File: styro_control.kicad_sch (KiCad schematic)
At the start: 89 parts, among them J3 INPUT_PEDAL, Q1 IRF7324, SW1 SW_RESET, SW2 switch_6_pin, SW3 SW_1, SW4 SW_2, SW5 SW_3, U1 STUSB4500QTR, U2 PAC1932-4, U3 ATSAMD21E18A-M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

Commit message: updated schematic
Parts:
- added D? (x3): LED, symbol Device:LED
- added D?: (no value), symbol Device:LED
- added RN?: R_Pack04, Resistor_SMD:R_Array_Convex_4x0603, symbol Device:R_Pack04
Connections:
- net GND: now also D?.1 (K), D?.1 (K), D?.1 (K), D?.1 (K)
- net TX_A6: now also RN?.4 (R4.1)
- net VBUS: now also RN?.1 (R1.1)
- net VSNK: now also RN?.2 (R2.1)
- new net: D?.2 (A), RN?.8 (R1.2)
- new net: D?.2 (A), RN?.7 (R2.2)
- new net: D?.2 (A), RN?.6 (R3.2)
- new net: D?.2 (A), RN?.5 (R4.2)
- new net +3.3V: RN?.3 (R3.1)
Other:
- moved on the sheet: C10, C11, C8, C9, R11, R12, R13, R14, R15, R16, R17, R18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

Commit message: added footprints
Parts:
- D11, D8, D9: renamed from D?; value LED -> (none)
- gave numbers to parts that had none: 3

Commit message: added footprints
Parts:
- added R7, R8: (no value), Resistor_SMD:R_0603_1608Metric, symbol Device:R
- R11, R12, R13, R14, R15, R16, R17, R18, R43, R44, R45, R46: footprint Resistor_SMD:R_0805_2012Metric_Pad1.15x1.40mm_HandSolder -> (none)
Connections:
- net GND: now also R7.1, R8.1; no longer D3.1 (RK), D3.3 (BK)
- new net: D3.1 (RK), R8.2
- new net: D3.3 (BK), R7.2
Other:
- note added: "x footprint von PAC1934 ändern >> größeres qfn!! x I2c Display pin reihenfolge ändern > VDD GND SCK SDA"
- note removed: "x footprint von PAC1934 ändern >> größeres qfn!! I2c Display pin reihenfolge ändern > VDD GND SCK SDA"
- moved on the sheet: D3

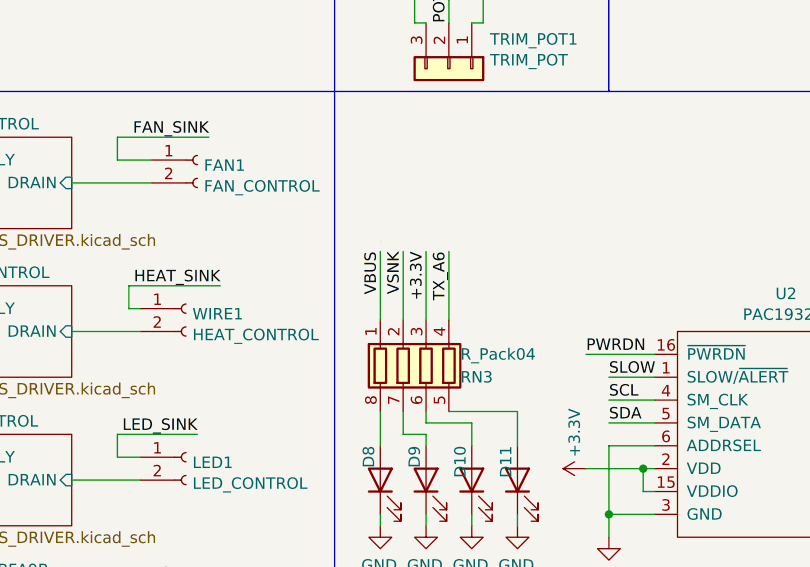
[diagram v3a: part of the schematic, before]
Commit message: added LEDs for VBUS,VSNK,3V3,TX
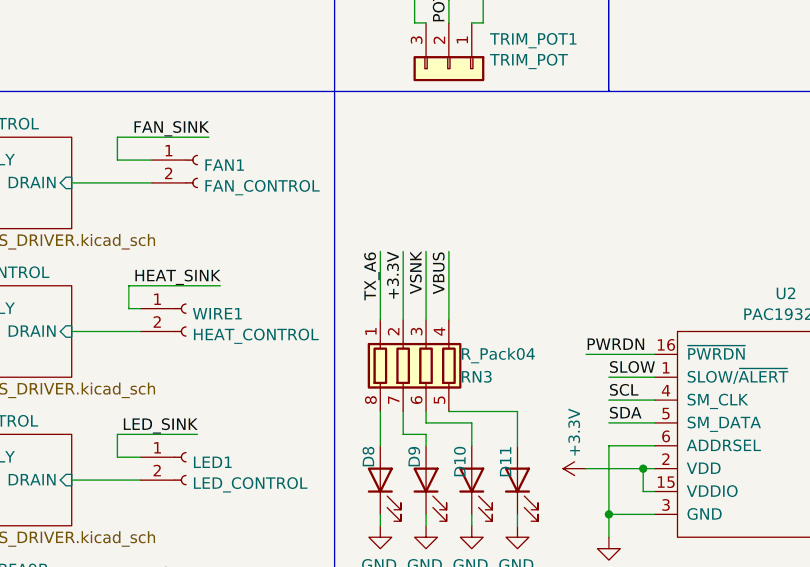
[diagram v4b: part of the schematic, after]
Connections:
- net +3.3V: now also RN3.2 (R2.1); no longer RN3.3 (R3.1)
- net TX_A6: now also RN3.1 (R1.1); no longer RN3.4 (R4.1)
- net VBUS: now also RN3.4 (R4.1); no longer RN3.1 (R1.1)
- net VSNK: now also RN3.3 (R3.1); no longer RN3.2 (R2.1)
